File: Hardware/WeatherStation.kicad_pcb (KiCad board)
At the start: 2 copper layers, 46 x 50 mm, 5 parts, among them J1 Conn_01x08, J2 Conn_01x08, J3 Conn_01x04, J4 Barrel_Jack_Switch, U1 TSR_1-2450

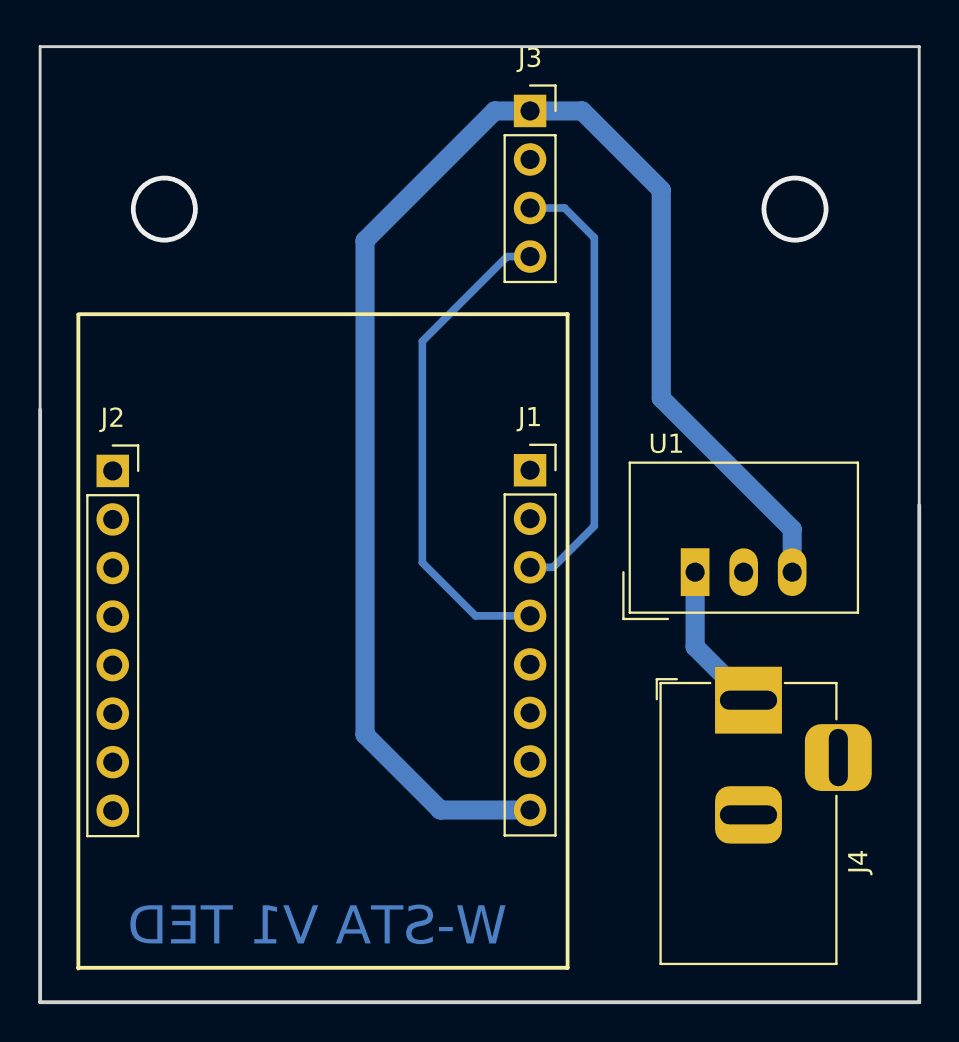
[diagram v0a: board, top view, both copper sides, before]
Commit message: Hardware changes
Added power and status LED, removed 1 screw hole
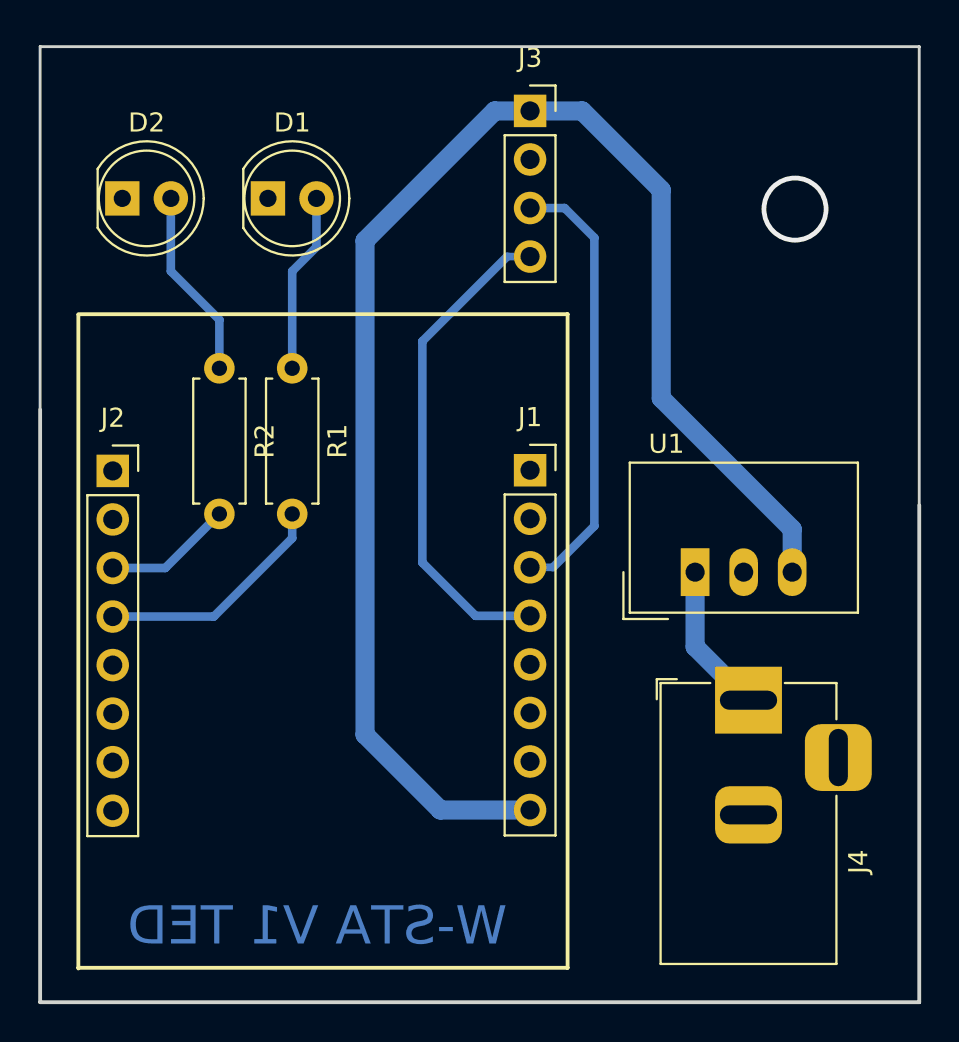
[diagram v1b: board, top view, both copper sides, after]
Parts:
- added D1: LED, LED_THT:LED_D5.0mm, F.Cu at (121.9, 27.9)
- added D2: LED, LED_THT:LED_D5.0mm, F.Cu at (114.3, 27.9)
- added R1: R, Resistor_THT:R_Axial_DIN0207_L6.3mm_D2.5mm_P7.62mm_Horizontal, F.Cu at (123.2, 36.8)
- added R2: R, Resistor_THT:R_Axial_DIN0207_L6.3mm_D2.5mm_P7.62mm_Horizontal, F.Cu at (119.4, 36.8)
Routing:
- net Net-(J2-Pad4): track 0.00 -> 12.4 mm
- net Net-(D2-Pad2): track 0.00 -> 9.94 mm
- net Net-(D1-Pad2): track 0.00 -> 9.42 mm
- net Net-(J2-Pad3): track 0.00 -> 6.75 mm
- net (no net): vias 2 -> 1
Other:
- net class Track: trace_width 0.4 -> 0.45
